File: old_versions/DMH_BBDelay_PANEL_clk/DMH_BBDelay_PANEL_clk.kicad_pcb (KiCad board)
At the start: 2 copper layers, 100 x 200 mm, 38 parts, among them J0 Panel_GND_Solder_Wire_Pad

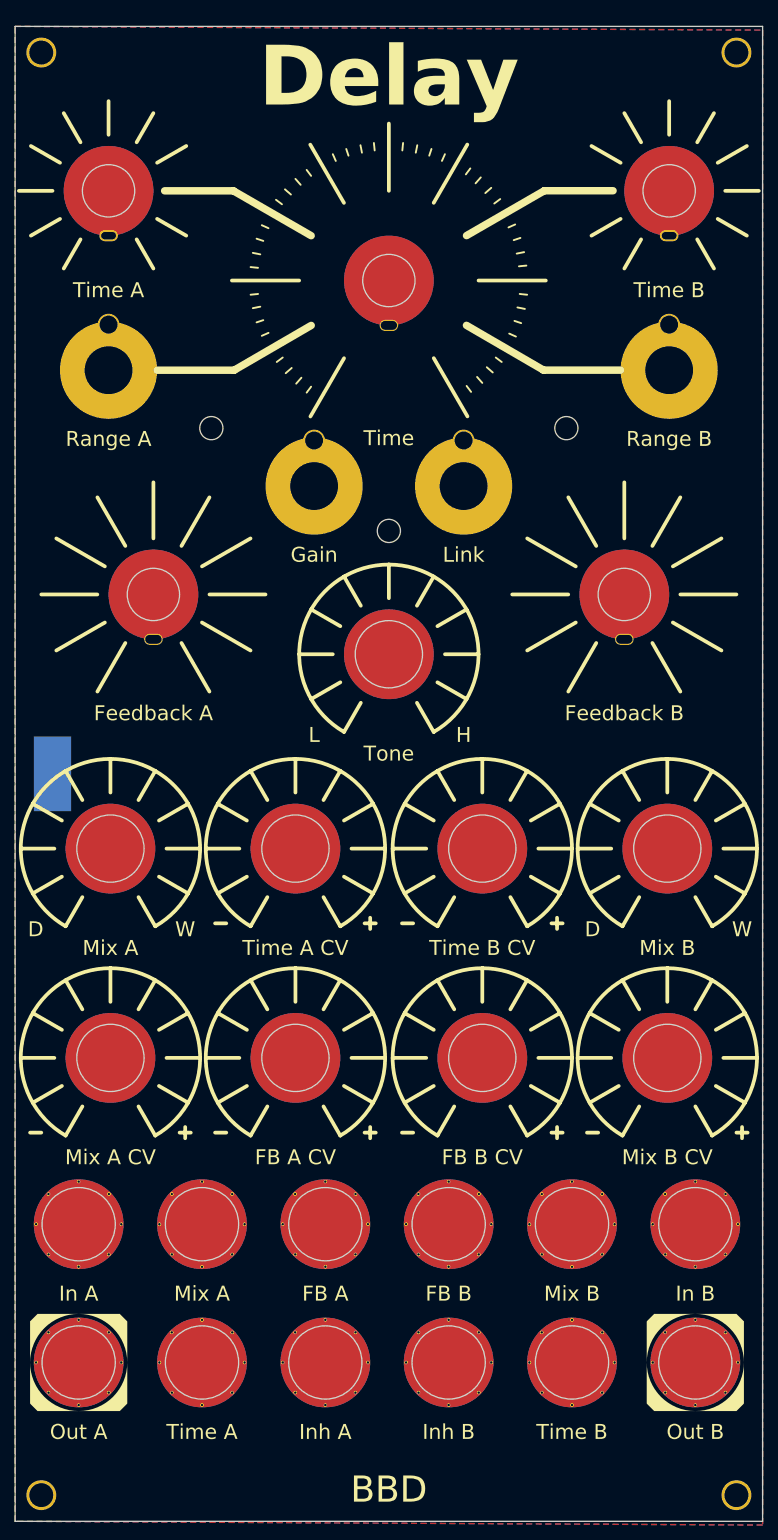
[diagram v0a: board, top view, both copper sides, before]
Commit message: Replaced Clock Sync with Inhibit input and Range
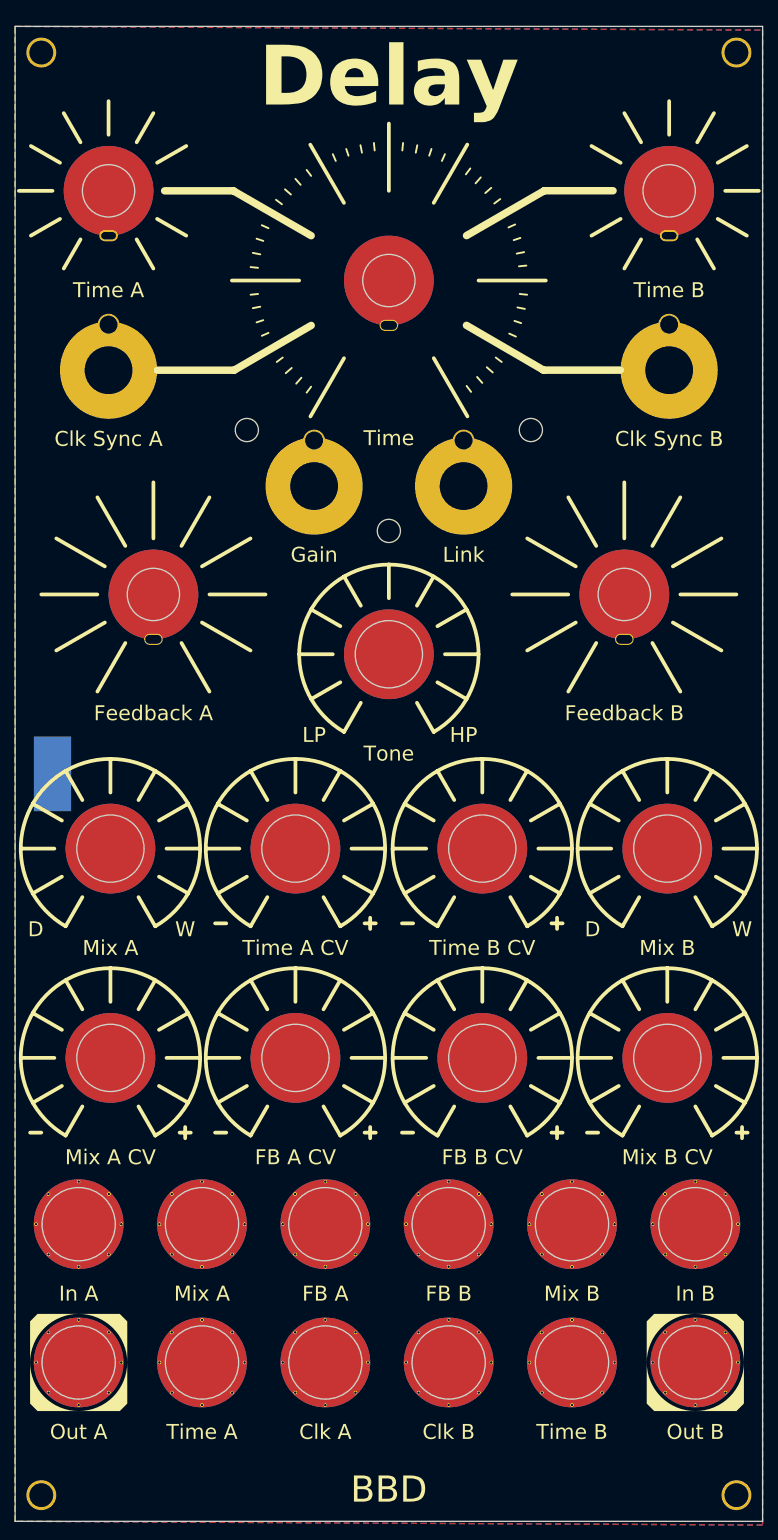
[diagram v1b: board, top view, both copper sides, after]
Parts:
- H18: value Range A -> Clk Sync A
- H19: value Range B -> Clk Sync B
- H34: value Inh A -> Clk A
- H35: value Inh B -> Clk B
- moved H28 4.76 mm to (81.0, 84.0)
- moved H29 4.76 mm to (119.0, 84.0)
